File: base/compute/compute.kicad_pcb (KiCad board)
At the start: 4 copper layers, 87.5 x 65.6 mm, 107 parts, among them IC1 TMC2209-LA-T, IC2 TMC2209-LA-T, IC3 TMC2209-LA-T, J1 USB_C_Receptacle_USB2.0_16P, J2 Conn_01x20, J3 2-84952-0, J4 Conn_01x02, J5 2-84952-0, Q1 Q_Dual_PMOS_S1G1S2G2D2D2D1D1, SW1 SW_Push_Open, SW2 SW_Push_Open, U1 MCP1700T-1202ETT, U2 ESP32-S3-WROOM-2, U3 LD1117S33TR_SOT223, U4 LM7805_TO263, U5 ICE40UP5K-SG48ITR-FPGA_Lattice, U6 MCP1700T-2802E, U7 USBLC6-2SC6

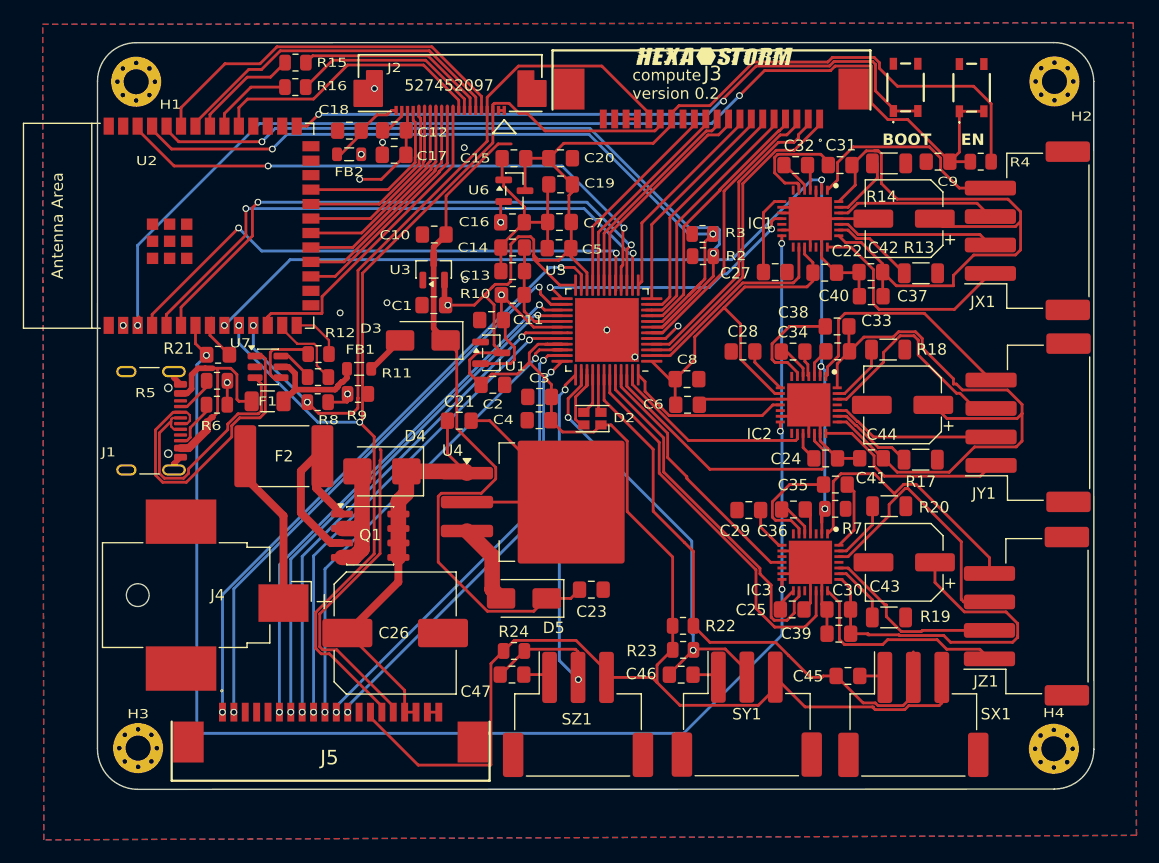
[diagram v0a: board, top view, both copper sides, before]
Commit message: board passes all tests
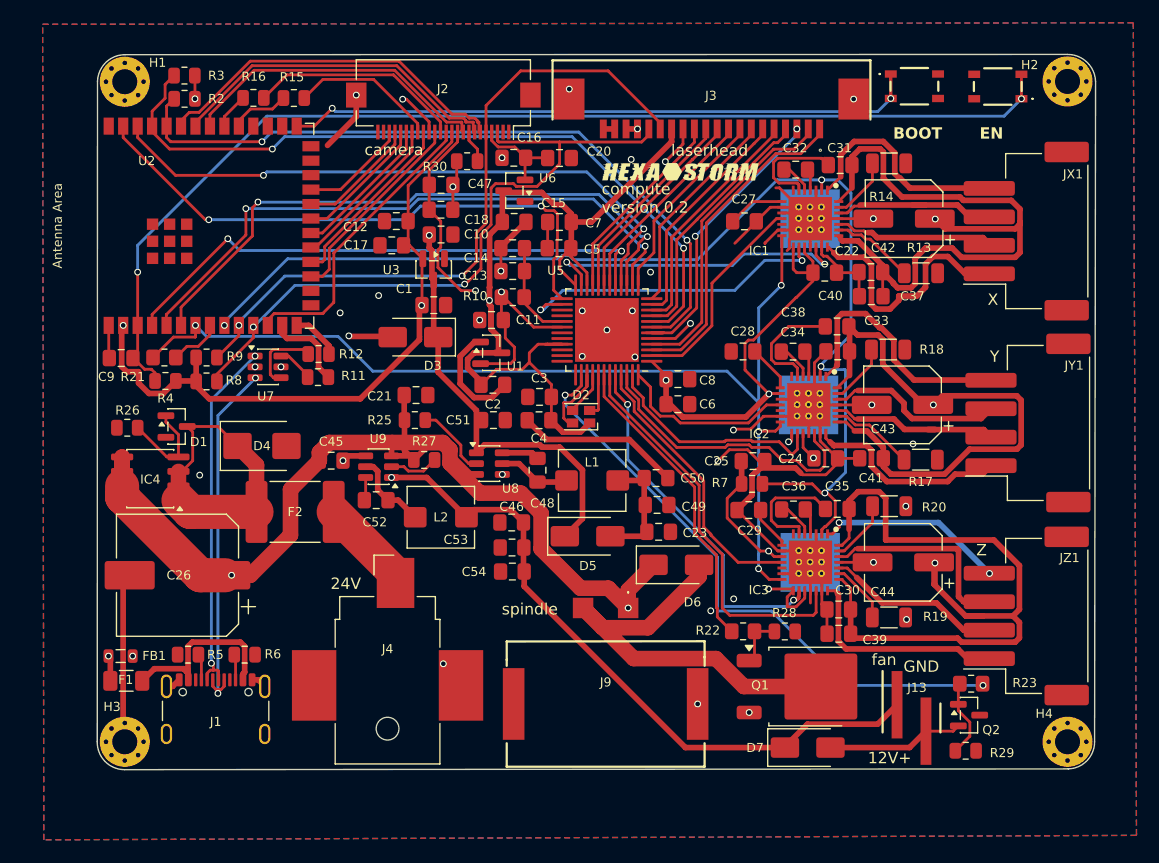
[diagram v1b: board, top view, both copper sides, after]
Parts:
- removed C19: 0.1uF, Capacitor_SMD:C_0805_2012Metric_Pad1.18x1.45mm_HandSolder
- removed FB2: 600R / 1.5A @ 100MHz, Inductor_SMD:L_0805_2012Metric
- removed J5: 2-84952-0, footprints:2-84952-0
- removed R24: 10K, Resistor_SMD:R_0805_2012Metric
- removed SX1, SY1, SZ1: Switch, footprints:JST_XH_S3B-XH-SM4-TB_1x03-1MP_P2.50mm_Horizontal
- removed U4: LM7805_TO263, Package_TO_SOT_SMD:TO-263-3_TabPin2
- added C48: 0.1uF, Capacitor_SMD:C_0805_2012Metric_Pad1.18x1.45mm_HandSolder, F.Cu at (209.7, 168.0)
- added C49: 10uF, Capacitor_SMD:C_0805_2012Metric_Pad1.18x1.45mm_HandSolder, F.Cu at (220.2, 171.1)
- added C50: 10uF, Capacitor_SMD:C_0805_2012Metric_Pad1.18x1.45mm_HandSolder, F.Cu at (220.1, 168.7)
- added C51: 10uF, Capacitor_SMD:C_0805_2012Metric_Pad1.18x1.45mm_HandSolder, F.Cu at (205.8, 163.6)
- added C52: 0.1uF, Capacitor_SMD:C_0805_2012Metric_Pad1.18x1.45mm_HandSolder, F.Cu at (195.5, 170.6)
- added C53: 10uF, Capacitor_SMD:C_0805_2012Metric_Pad1.18x1.45mm_HandSolder, F.Cu at (207.4, 174.8)
- added C54: 10uF, Capacitor_SMD:C_0805_2012Metric_Pad1.18x1.45mm_HandSolder, F.Cu at (207.5, 176.9)
- added D1: D_Zener, Package_TO_SOT_SMD:SOT-23, F.Cu at (178.0, 164.2)
- added D6: D_Schottky, Diode_SMD:D_SMA, F.Cu at (221.9, 176.3)
- added D7: SS24FL, Diode_SMD:D_SMA, F.Cu at (233.4, 192.4)
- added IC4: DMP6023LSS-13, Package_SO:SOIC-8_3.9x4.9mm_P1.27mm, F.Cu at (175.7, 168.7)
- added J13: fan, footprints:TSM-102-01-L-SV, F.Cu at (242.5, 189.8)
- added J9: spindle, footprints:21548291, F.Cu at (215.7, 188.5)
- added L1: 10uH, Inductor_SMD:L_Bourns_SRP5030T, F.Cu at (214.5, 168.9)
- added L2: 10uH, Inductor_SMD:L_Bourns_SRP5030T, F.Cu at (201.2, 172.1)
- added Q2: Q_NMOS_GDS_fan, Package_TO_SOT_SMD:SOT-23, F.Cu at (247.6, 189.5)
- added R25: 10K, Resistor_SMD:R_0805_2012Metric, F.Cu at (198.9, 163.6)
- added R26: 10K, Resistor_SMD:R_0805_2012Metric, F.Cu at (173.6, 164.3)
- added R27: 10K, Resistor_SMD:R_0805_2012Metric, F.Cu at (199.7, 167.1)
- added R28: 10K, Resistor_SMD:R_0805_2012Metric, F.Cu at (231.4, 182.2)
- added R29: 10K, Resistor_SMD:R_0805_2012Metric, F.Cu at (247.3, 192.6)
- added R30: 10K, Resistor_SMD:R_0805_2012Metric, F.Cu at (203.5, 140.9)
- added U8: AP63205WU-7, Package_TO_SOT_SMD:TSOT-23-6, F.Cu at (205.4, 167.4)
- added U9: AP63203WU-7, Package_TO_SOT_SMD:TSOT-23-6, F.Cu at (195.7, 167.7)
- C45, C46, C47: value 0.1uF -> 10uF
- F1: value Fuse -> 8V 1.1A
- F2: value Fuse -> 24V 3.0A
- J2: footprint footprints:CON_527452097_MOL -> Connector_FFC-FPC:Hirose_FH12-24S-0.5SH_1x24-1MP_P0.50mm_Horizontal
- J4: value Conn_01x02 -> power
- Q1: value Q_Dual_PMOS_S1G1S2G2D2D2D1D1 -> Q_NMOS_GDS_spindle; footprint Package_SO:SOIC-8_3.9x4.9mm_P1.27mm -> Package_TO_SOT_SMD:TO-252-2
- R22, R23: value 10K -> 100; footprint Resistor_SMD:R_0805_2012Metric -> Resistor_SMD:R_0805_2012Metric_Pad1.20x1.40mm_HandSolder
- moved R4 74.2 mm to (177.0, 160.2)
- moved C9 73.8 mm to (173.1, 158.2)
- moved C45 49.2 mm to (191.5, 167.2)
- moved R2 47.6 mm to (178.7, 135.4), turned to 180 degrees
- moved R3 47.6 mm to (178.7, 133.3), turned to 0 degrees
- moved C47 43.5 mm to (201.2, 142.9)
- moved Q1 40.5 mm to (233.3, 187.0)
- moved FB1 32.8 mm to (173.1, 184.3)
- moved F1 27.5 mm to (173.6, 186.5), turned to 180 degrees
- moved J1 27.3 mm to (181.4, 190.1), turned to 0 degrees
- moved R23 25.5 mm to (247.8, 186.8)
- moved R5 24.2 mm to (179.0, 184.2), turned to 180 degrees
- moved R6 22.1 mm to (183.9, 184.2)
- moved C46 20.0 mm to (207.4, 172.6), turned to 180 degrees
- moved C26 19.8 mm to (178.1, 177.2), turned to 180 degrees
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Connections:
- C12 pad 1: +2V8 -> +3.3V
- C17 pad 1: +2V8 -> +3.3V
- C18 pad 1: Net-(J2-Pin_20) -> +1V2
- C20 pad 1: +3.3V -> +2V8
- C21 pad 1: +12V -> +24V
- C23 pad 1: +5V -> Net-(D5-A)
- C26 pad 1: +12V -> +24V
- C30 pad 2: +12V -> +24V
- C31 pad 2: +12V -> +24V
- C33 pad 2: +12V -> +24V
- C35 pad 2: +12V -> +24V
- C37 pad 2: +12V -> +24V
- C38 pad 2: +12V -> +24V
- C39 pad 2: +12V -> +24V
- C40 pad 2: +12V -> +24V
- C41 pad 2: +12V -> +24V
- C42 pad 1: +12V -> +24V
- C43 pad 1: +12V -> +24V
- C44 pad 1: +12V -> +24V
- C45 pad 1: X_PO -> +24V
- C46 pad 1: Y_PO -> +12V
- C47 pad 1: Z_PO -> +1V2
- D4 pad 1: +12V -> Net-(D4-A1)
- F2 pad 1: Net-(Q1A-S) -> Net-(D4-A1)
- IC1 pad 22: +12V -> +24V
- IC1 pad 28: +12V -> +24V
- IC2 pad 22: +12V -> +24V
- IC2 pad 28: +12V -> +24V
- IC3 pad 22: +12V -> +24V
- IC3 pad 28: +12V -> +24V
- J2 pad 1: GND -> unconnected-(J2-Pin_1-Pad1)
- J2 pad 10: D6 -> +1V2
- J2 pad 11: D5 -> +3.3V
- J2 pad 12: D4 -> DVP_Y9
- J2 pad 13: D3 -> Net-(J2-Pin_13)
- J2 pad 14: D2 -> DVP_Y8
- J2 pad 15: D1 -> GND
- J2 pad 16: D0 -> DVP_Y7
- J2 pad 17: CAM_RST -> Net-(J2-Pin_17)
- J2 pad 18: GND -> DVP_Y6
- J2 pad 19: +2V8 -> DVP_Y2
- J2 pad 20: Net-(J2-Pin_20) -> DVP_Y5
- J2 pad 3: SCL -> SDA
- J2 pad 4: SDA -> +2V8
- J2 pad 5: VSYNC -> SCL
- J2 pad 6: HSYNC -> CAM_RST
- J2 pad 7: Net-(J2-Pin_7) -> VSYNC
- J2 pad 9: D7 -> HREF
- J3 pad MP: unconnected-(J3-MountPin-PadMP) -> GND
- JX1 pad MP: unconnected-(JX1-MountPin-PadMP)_1 -> GND
- JY1 pad MP: unconnected-(JY1-MountPin-PadMP)_1 -> GND
- JZ1 pad MP: unconnected-(JZ1-MountPin-PadMP) -> GND
- Q1 pad 1: Net-(Q1A-S) -> Net-(Q1-G)
- Q1 pad 2: GND -> Net-(D6-A)
- Q1 pad 3: Net-(Q1A-S) -> GND
- R15 pad 2: Net-(J2-Pin_7) -> Net-(J2-Pin_17)
- R16 pad 1: Net-(J2-Pin_8) -> Net-(J2-Pin_13)
- R22 pad 1: +3.3V -> Net-(Q1-G)
- R22 pad 2: X_PO -> SPINDLE
- R23 pad 1: +3.3V -> Net-(Q2-G)
- R23 pad 2: Y_PO -> FAN
- U2 pad 12: D6 -> DVP_Y9
- U2 pad 17: D5 -> DVP_Y8
- U2 pad 18: D4 -> DVP_Y7
- U2 pad 19: D3 -> DVP_Y6
- U2 pad 20: D2 -> DVP_Y2
- U2 pad 21: D1 -> DVP_Y5
- U2 pad 22: D0 -> DVP_Y3
- U2 pad 23: CAM_RST -> DVP_Y4
- U2 pad 31: D7 -> PCLK
- U2 pad 33: PCLK -> HREF
- U2 pad 34: HSYNC -> VSYNC
- U2 pad 35: VSYNC -> CAM_RST
- U2 pad 39: unconnected-(U2-GPIO1/TOUCH1/ADC1_CH0-Pad39) -> FIFO_FULL
- U5 pad 2: X_STEP -> DIAG_X
- U5 pad 23: FPGA37 -> X_DIR
- U5 pad 25: DIAG_X -> FIFO_FULL
- U5 pad 26: FPGA39 -> X_STEP
- U5 pad 27: FPGA38 -> unconnected-(U5A-IOT_38b-Pad27)
- U5 pad 28: FPGA41 -> unconnected-(U5A-IOT_41a-Pad28)
- U5 pad 31: FPGA42 -> unconnected-(U5A-IOT_42b-Pad31)
- U5 pad 32: FPGA43 -> unconnected-(U5A-IOT_43a-Pad32)
- U5 pad 34: FPGA44 -> unconnected-(U5A-IOT_44b-Pad34)
- U5 pad 35: FPGA46 -> unconnected-(U5A-IOT_46b_G0-Pad35)
- U5 pad 36: FPGA48 -> unconnected-(U5A-IOT_48b-Pad36)
- U5 pad 37: Z_PO -> unconnected-(U5A-IOT_45a_G1-Pad37)
- U5 pad 38: Y_PO -> FAN
- U5 pad 42: X_PO -> SPINDLE
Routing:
- net +24V: track 0.00 -> 462.4 mm, vias 0 -> 5
- net +12V: track 192.9 -> 107.8 mm, vias 0 -> 2
- net +3.3V: track 338.1 -> 272.2 mm, vias 3 -> 10
- net FPGA37: track 55.8 -> 0.00 mm, vias 2 -> 0
- net FAN: track 0.00 -> 53.3 mm, vias 0 -> 2
- net FPGA39: track 52.3 -> 0.00 mm, vias 2 -> 0
- net X_PO: track 51.8 -> 0.00 mm
- net FIFO_FULL: track 0.00 -> 51.7 mm, vias 0 -> 2
- net FPGA38: track 47.4 -> 0.00 mm, vias 2 -> 0
- net FPGA41: track 46.2 -> 0.00 mm, vias 2 -> 0
- net FPGA43: track 44.9 -> 0.00 mm, vias 2 -> 0
- net FPGA42: track 44.7 -> 0.00 mm, vias 2 -> 0
- net FPGA44: track 42.8 -> 0.00 mm, vias 2 -> 0
- net FPGA46: track 41.4 -> 0.00 mm, vias 2 -> 0
- net FPGA48: track 39.6 -> 0.00 mm, vias 2 -> 0
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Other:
- board size 87.5 x 65.6 mm -> 87.7 x 62.8 mm
- board text added: "12V+"
- board text added: "24V"
- board text added: "GND"
- board text added: "X"
- board text added: "Y"
- board text added: "Z"
- board text added: "camera"
- board text added: "fan"
- board text added: "laserhead"
- board text added: "spindle"
